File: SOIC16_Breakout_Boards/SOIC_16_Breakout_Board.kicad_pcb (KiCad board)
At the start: 2 copper layers, 25 x 25 mm, 6 parts, among them J1 Conn_01x04, J2 Conn_01x04, J3 Conn_01x01, J4 Conn_01x01

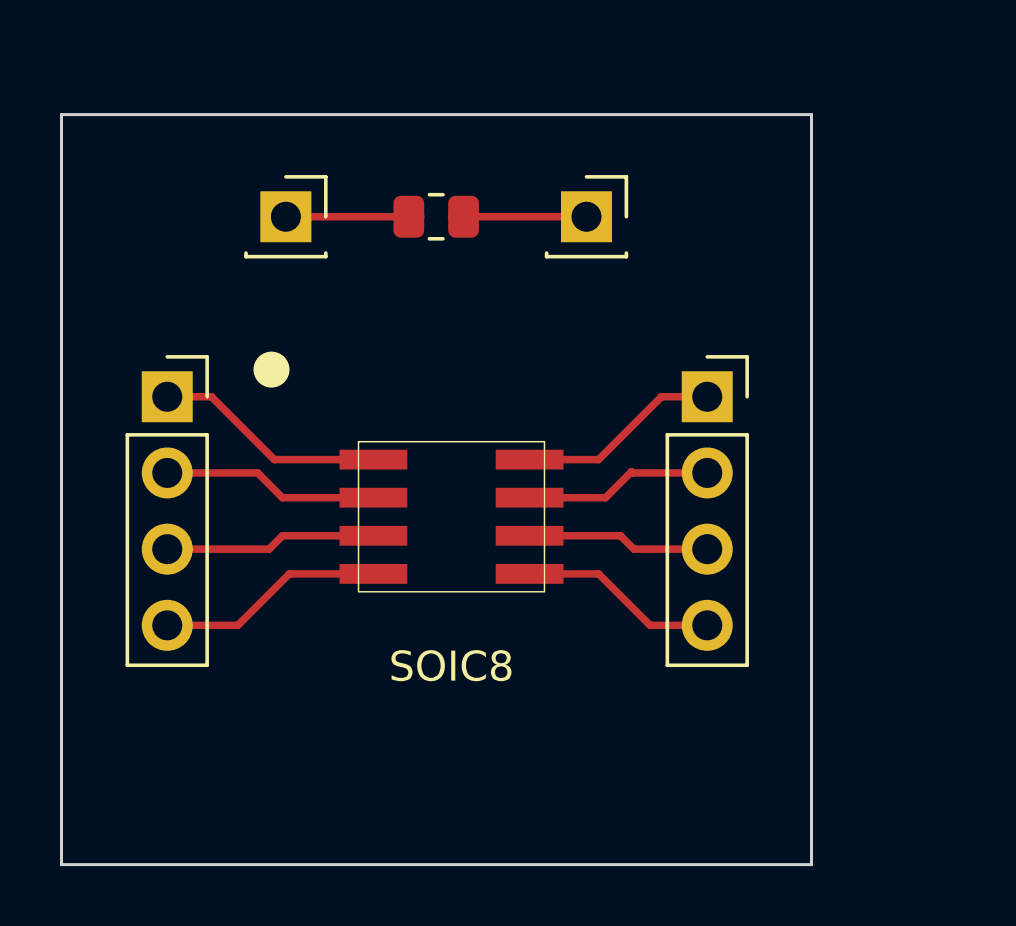
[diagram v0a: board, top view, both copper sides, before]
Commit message: Created PCB designs for the 14, 16 & 20 pic SOIC's
Finalized and committed pcb designs for the 14, 16, and 20 SOIC breakout boards
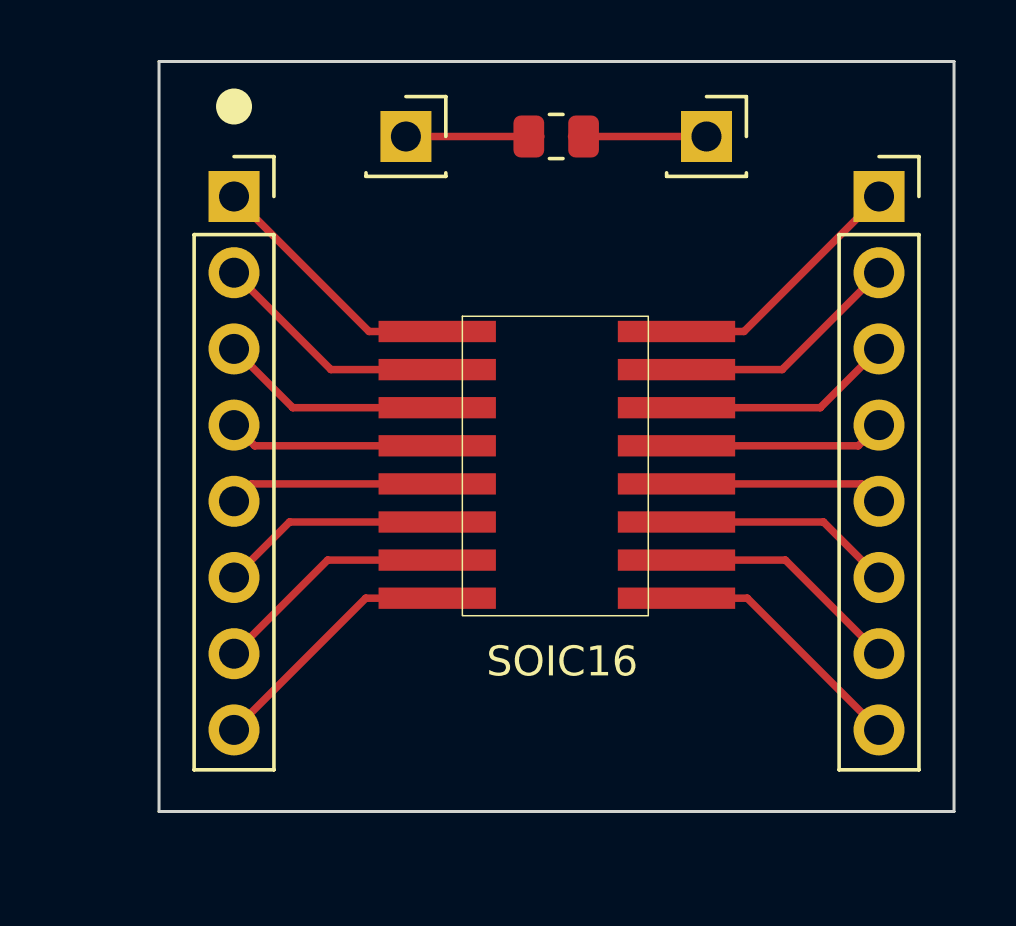
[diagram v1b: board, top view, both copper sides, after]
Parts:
- removed SOIC8: 8_Pin_SOIC_Board, SOIC_Footprints:8_Pin_SOIC_Board
- added SOIC16: 16_Pin_SOIC_Board, SOIC_Footprints:16_Pin_SOIC_Board, F.Cu at (158.7, 99.5)
- J1, J2: value Conn_01x04 -> Conn_01x08; footprint Connector_PinSocket_2.54mm:PinSocket_1x04_P2.54mm_Vertical -> Connector_PinSocket_2.54mm:PinSocket_1x08_P2.54mm_Vertical
- moved J2 8.79 mm to (169.3, 90.7)
- moved J1 7.04 mm to (147.8, 90.7)
- moved J3 4.81 mm to (163.5, 88.7)
- moved J4 4.81 mm to (153.5, 88.7)
- moved R1 4.81 mm to (158.5, 88.7)
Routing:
- net Net-(J1-Pad8): track 0.00 -> 8.59 mm
- net Net-(J2-Pad8): track 0.00 -> 8.57 mm
- net Net-(J1-Pad7): track 0.00 -> 8.07 mm
- net Net-(J2-Pad7): track 0.00 -> 8.04 mm
- net Net-(J1-Pad6): track 0.00 -> 7.54 mm
- net Net-(J2-Pad6): track 0.00 -> 7.52 mm
- net Net-(J1-Pad5): track 0.00 -> 7.01 mm
- net Net-(J2-Pad5): track 0.00 -> 6.99 mm
- net Net-(J1-Pad2): track 6.71 -> 8.11 mm
- net Net-(J1-Pad1): track 7.24 -> 8.64 mm
- net Net-(J2-Pad1): track 7.29 -> 8.61 mm
- net Net-(J2-Pad2): track 6.80 -> 8.09 mm
- net Net-(J1-Pad3): track 6.56 -> 7.59 mm
- net Net-(J2-Pad3): track 6.61 -> 7.56 mm
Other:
- board size 25 x 25 mm -> 26.5 x 25 mm
- board text added: "16 Pin SOIC Breakout Board"
- board text removed: "8 Pin SOIC Breakout Board"

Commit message: Fixed warnings on all SOIC boards
Ensured that silkscreen traces didn't intersect solder masks and name/board information is visible on the front of the board rather than the back
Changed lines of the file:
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@@
       (effects (font (size 1 1) (thickness 0.15)))
     )
-    (fp_rect (start -3.3274 -4.826) (end 2.8702 5.1562) (layer "F.SilkS") (width 0.05) (fill none))
-    (fp_rect (start -6.604 -4.953) (end 5.969 5.461) (layer "F.Fab") (width 0.12) (fill none))
+    (fp_rect (start -6.604 -4.953) (end 5.969 5.461) (layer "F.SilkS") (width 0.12) (fill none))
+    (fp_rect (start -3.3274 -4.826) (end 2.8702 5.1562) (layer "F.Fab") (width 0.05) (fill none))
     (pad "1" smd rect (at -4.1656 -4.318) (size 3.9116 0.7112) (layers "F.Cu" "F.Paste" "F.Mask")
       (net 3 "Net-(J1-Pad1)") (pintype "unspecified"))
@@
   (gr_circle (center 147.751 87.73) (end 148.251 87.73) (layer "F.SilkS") (width 0.2) (fill solid))
   (gr_rect (start 145.251 86.23) (end 171.751 111.23) (layer "Edge.Cuts") (width 0.1) (fill none))
-  (gr_text "16 Pin SOIC Breakout Board" (at 159.251 110.23) (layer "B.SilkS")
+  (gr_text "16 Pin SOIC Breakout Board" (at 159.251 110.23) (layer "F.SilkS")
     (effects (font (size 0.5 0.5) (thickness 0.05)))
   )
-  (gr_text "Jack Tillman" (at 158.251 109.23) (layer "B.SilkS")
+  (gr_text "Jack Tillman" (at 158.251 109.23) (layer "F.SilkS")
     (effects (font (size 0.5 0.5) (thickness 0.05)))
   )

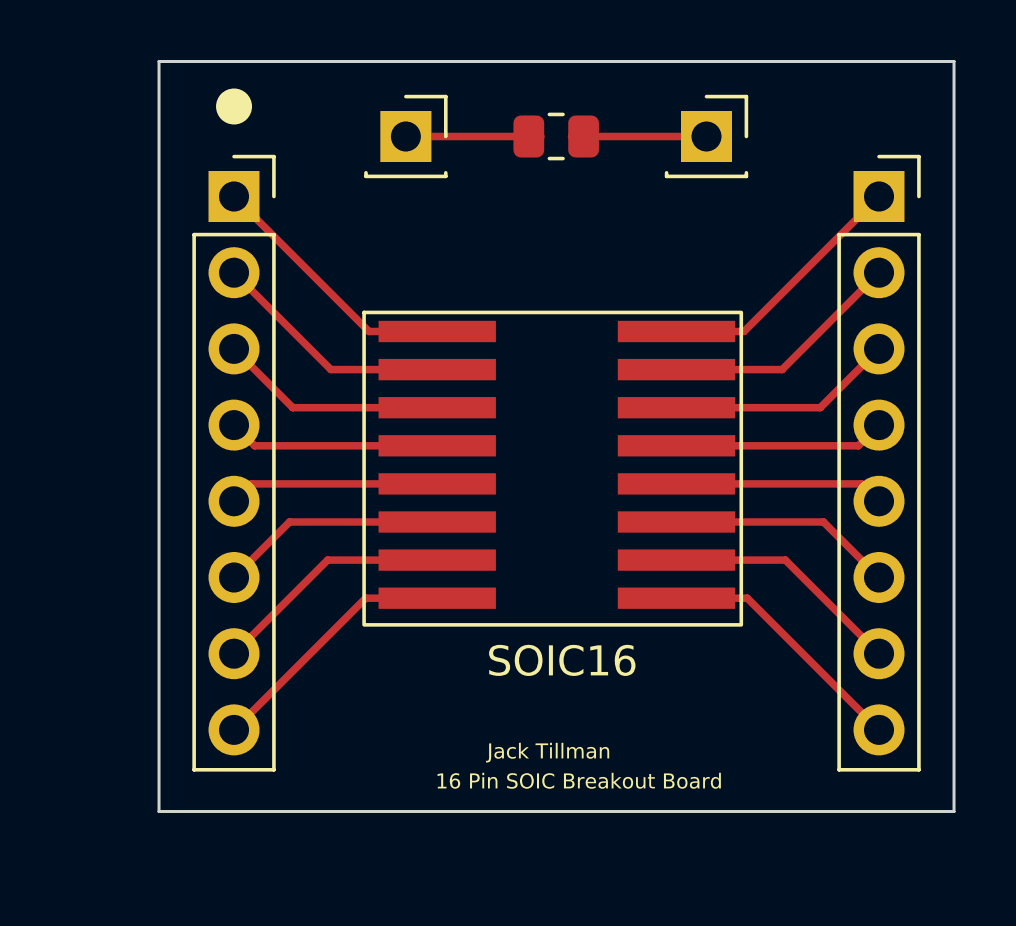
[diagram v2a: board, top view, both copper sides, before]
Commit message: Finished tracing the SOIC20 board
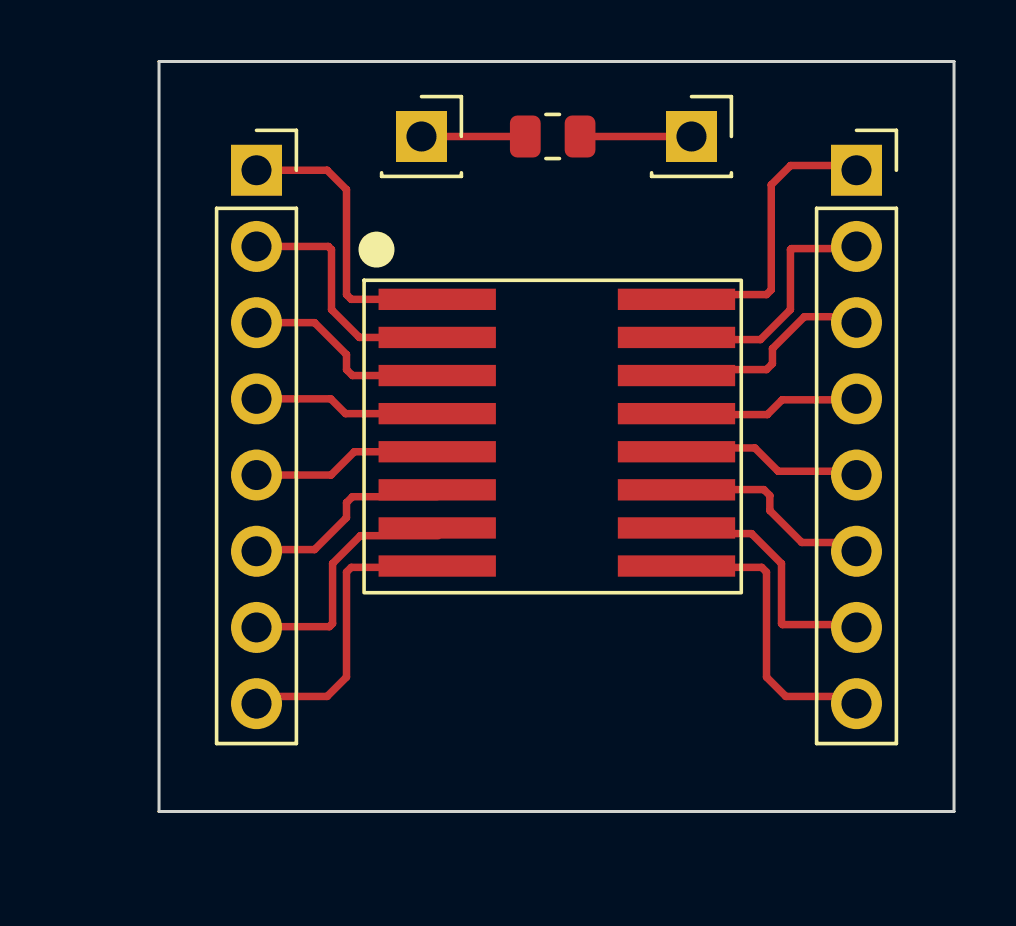
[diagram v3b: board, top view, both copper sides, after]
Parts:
- moved J2 1.15 mm to (168.5, 89.9)
- moved J1 1.15 mm to (148.5, 89.9)
- moved SOIC16 1.07 mm to (158.7, 98.5)
- moved J4 0.52 mm to (154.0, 88.7)
- moved J3 0.50 mm to (163.0, 88.7)
- moved R1 0.12 mm to (158.4, 88.7)
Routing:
- net Net-(J2-Pad8): track 8.57 -> 9.86 mm
- net Net-(J1-Pad8): track 8.59 -> 9.86 mm
- net Net-(J2-Pad1): track 8.61 -> 9.86 mm
- net Net-(J1-Pad1): track 8.64 -> 9.86 mm
- net Net-(J4-Pad1): track 4.50 -> 3.46 mm
- net Net-(J1-Pad4): track 7.06 -> 6.23 mm
- net Net-(J2-Pad4): track 7.04 -> 6.23 mm
- net Net-(J1-Pad5): track 7.01 -> 6.35 mm
- net Net-(J2-Pad5): track 6.99 -> 6.35 mm
- net Net-(J1-Pad3): track 7.59 -> 7.05 mm
- net Net-(J2-Pad3): track 7.56 -> 7.05 mm
